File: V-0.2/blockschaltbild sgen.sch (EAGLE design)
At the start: 0 parts

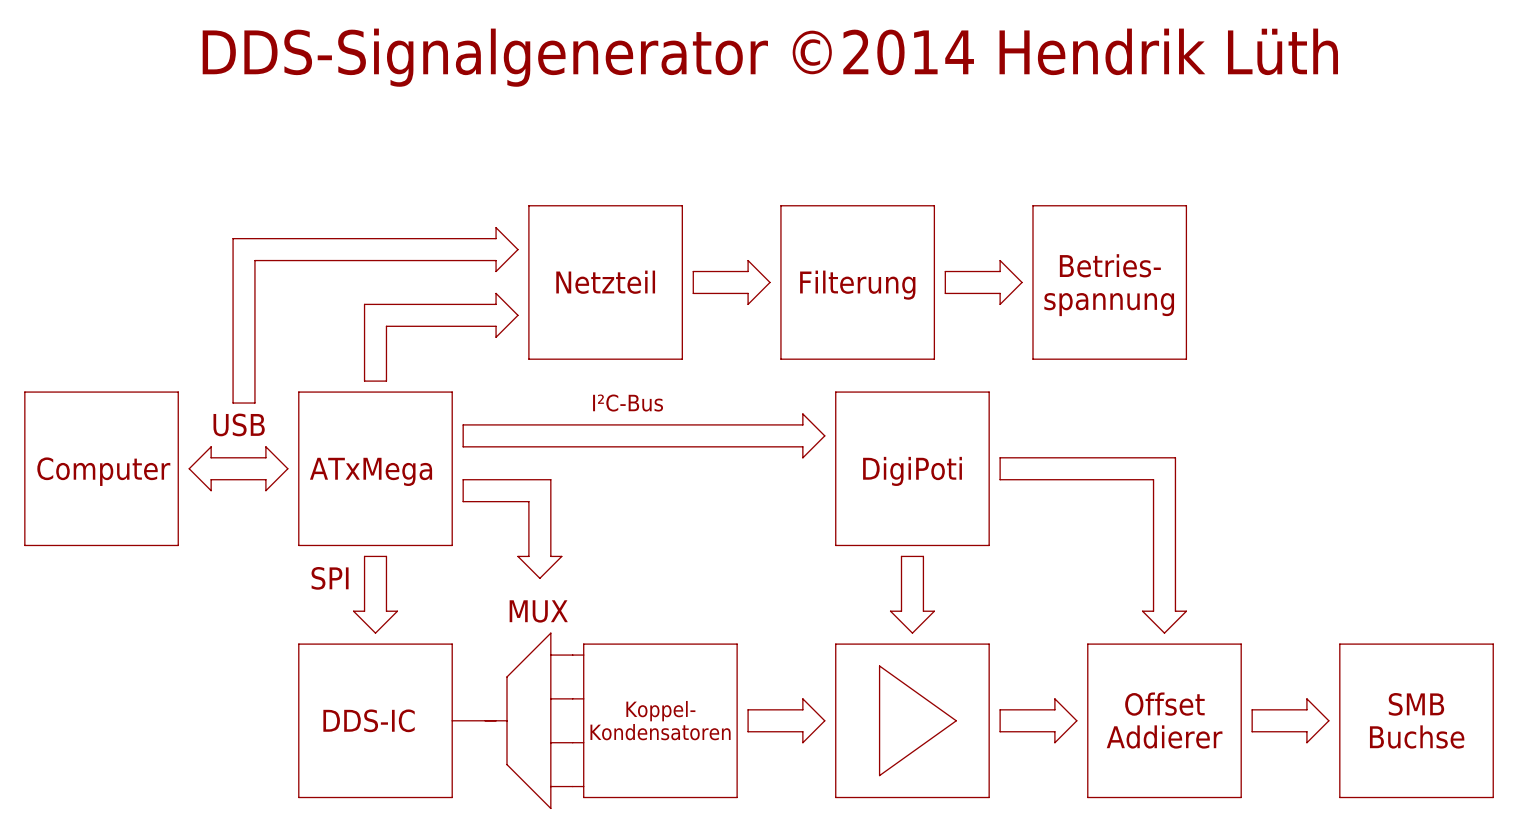
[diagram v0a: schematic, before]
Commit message: new circuit-diagramm, reorganized folder structure
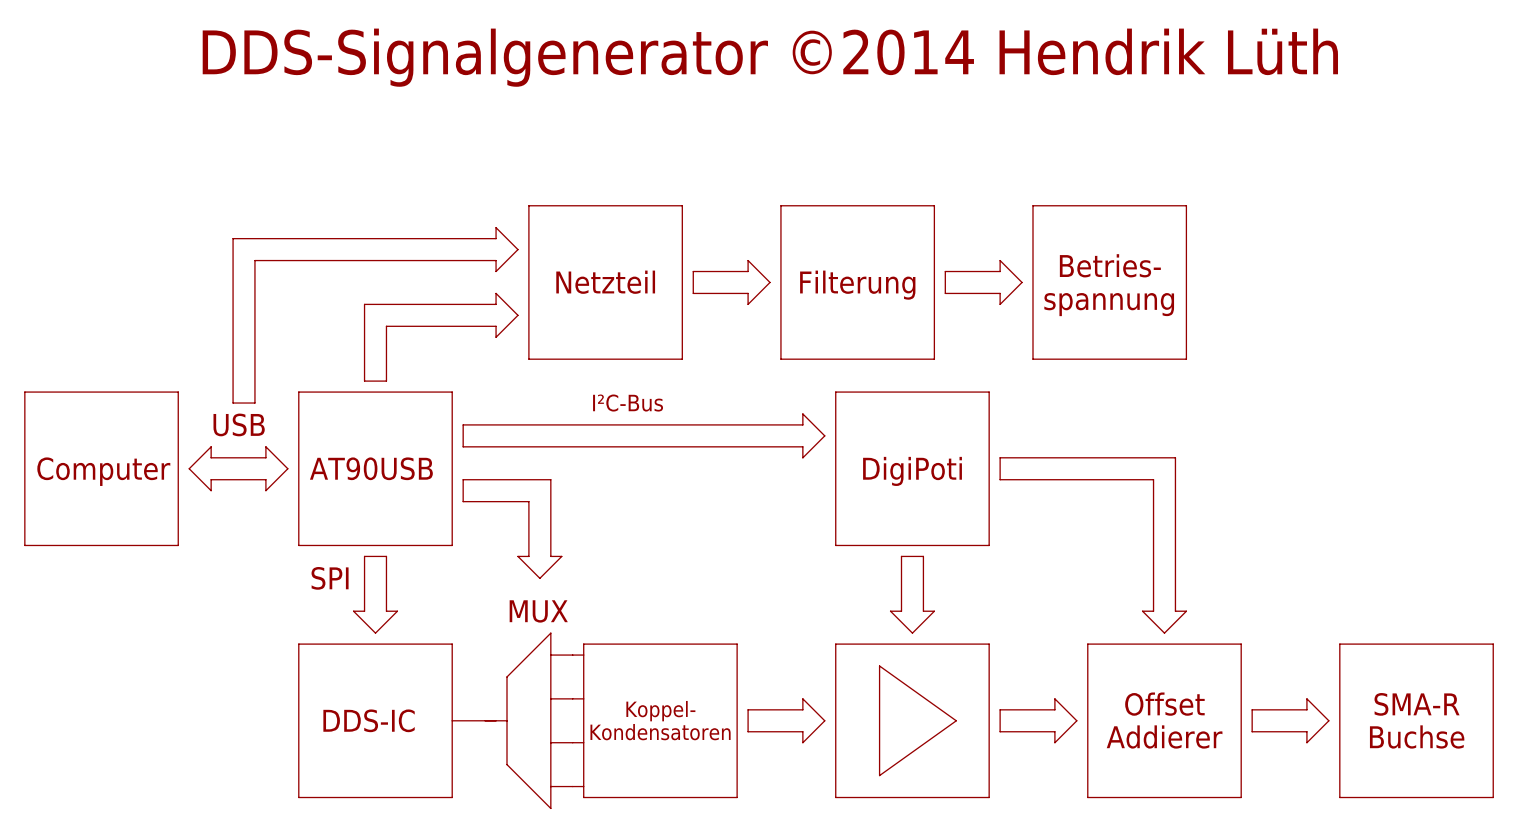
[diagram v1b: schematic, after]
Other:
- note added: "AT90USB"
- note added: "SMA-R Buchse"
- note removed: "ATxMega"
- note removed: "SMB Buchse"
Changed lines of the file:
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@@
 <text x="25.4" y="50.8" size="5.08" layer="94">Computer</text>
 <text x="66.04" y="60.96" size="5.08" layer="94">USB</text>
-<text x="88.9" y="50.8" size="5.08" layer="94">ATxMega</text>
+<text x="88.9" y="50.8" size="5.08" layer="94">AT90USB</text>
 <text x="91.44" y="-7.62" size="5.08" layer="94">DDS-IC</text>
 <text x="88.9" y="25.4" size="5.08" layer="94">SPI</text>
@@
 <wire x1="248.92" y1="55.88" x2="289.56" y2="55.88" width="0.3048" layer="94"/>
 <wire x1="289.56" y1="55.88" x2="289.56" y2="20.32" width="0.3048" layer="94"/>
-<text x="345.44" y="-5.08" size="5.08" layer="94" align="center">SMB
+<text x="345.44" y="-5.08" size="5.08" layer="94" align="center">SMA-R
 Buchse</text>
 <wire x1="101.6" y1="73.66" x2="106.68" y2="73.66" width="0.254" layer="94"/>
